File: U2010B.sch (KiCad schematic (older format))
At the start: 27 parts, among them J1 PHASE, J2 M2, J3 Rsh, J4 Rsh, J5 NULL, J6 M1, P1 50k, Q1 BT136-600, U1 U2010B

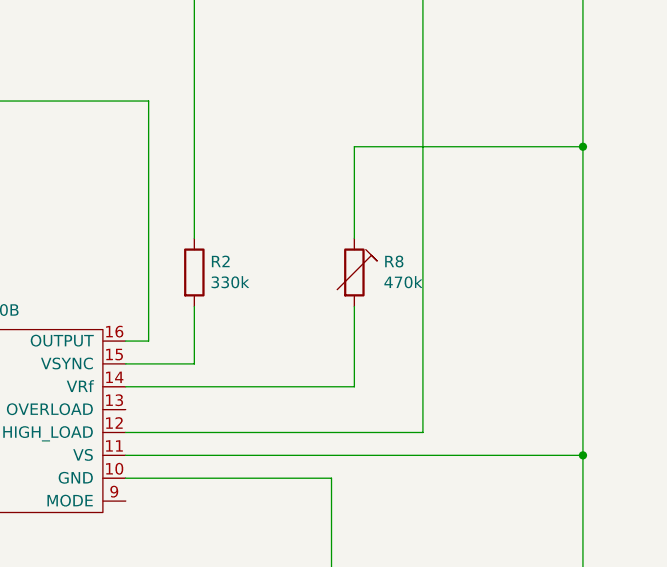
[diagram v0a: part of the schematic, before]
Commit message: Trace PCB
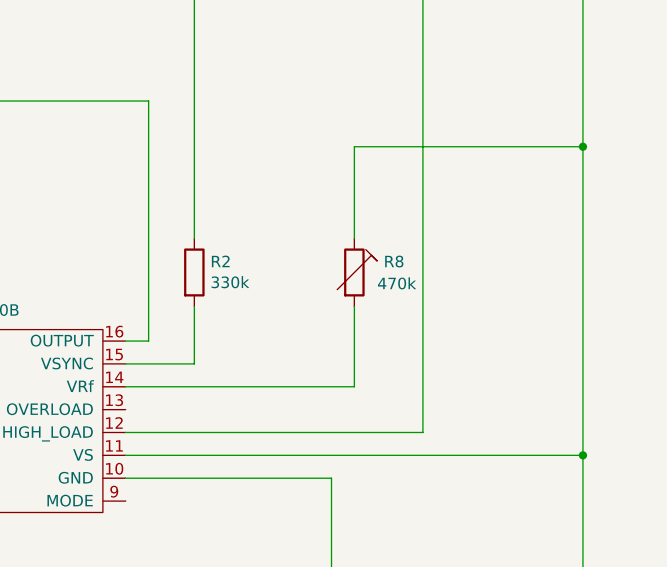
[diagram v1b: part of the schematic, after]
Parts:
- R10, R11, R8: footprint Potentiometer_THT:Potentiometer_Vishay_T7-YA_Single_Vertical -> Potentiometer_THT:Potentiometer_Bourns_3339P_Vertical_HandSoldering
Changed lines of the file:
@@
 P 7800 3350
 F 0 "R8" H 7928 3396 50  0000 L CNN
-F 1 "470k" H 7928 3305 50  0000 L CNN
-F 2 "Potentiometer_THT:Potentiometer_Vishay_T7-YA_Single_Vertical" V 7730 3350 50  0001 C CNN
+F 1 "470k" H 7900 3300 50  0000 L CNN
+F 2 "Potentiometer_THT:Potentiometer_Bourns_3339P_Vertical_HandSoldering" V 7730 3350 50  0001 C CNN
 F 3 "~" H 7800 3350 50  0001 C CNN
 	1    7800 3350
@@
 F 0 "R10" V 4150 5050 50  0000 C CNN
 F 1 "100k" V 4250 5100 50  0000 C CNN
-F 2 "Potentiometer_THT:Potentiometer_Vishay_T7-YA_Single_Vertical" V 3980 5150 50  0001 C CNN
+F 2 "Potentiometer_THT:Potentiometer_Bourns_3339P_Vertical_HandSoldering" V 3980 5150 50  0001 C CNN
 F 3 "~" H 4050 5150 50  0001 C CNN
 	1    4050 5150
@@
 F 0 "R11" V 4650 4300 50  0000 C CNN
 F 1 "1M" V 4650 4550 50  0000 C CNN
-F 2 "Potentiometer_THT:Potentiometer_Vishay_T7-YA_Single_Vertical" V 4680 4450 50  0001 C CNN
+F 2 "Potentiometer_THT:Potentiometer_Bourns_3339P_Vertical_HandSoldering" V 4680 4450 50  0001 C CNN
 F 3 "~" H 4750 4450 50  0001 C CNN
 	1    4750 4450

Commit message: Add netlist, change some pins for drill.
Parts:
- C1: footprint Capacitor_THT:CP_Radial_D6.3mm_P2.50mm -> Capacitor_THT:CP_Radial_D10.0mm_P3.80mm
- C2, C7: footprint Capacitor_THT:CP_Radial_D6.3mm_P2.50mm -> Capacitor_THT:CP_Radial_D8.0mm_P3.80mm
- D3: footprint LED_THT:LED_D3.0mm -> LED_THT:LED_D5.0mm
- J1, J2, J3, J4, J5, J6: footprint Connector_Pin:Pin_D1.0mm_L10.0mm -> Connector_Wire:SolderWirePad_1x01_Drill2mm
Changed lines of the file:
@@
 F 0 "D3" H 8443 2166 50  0000 C CNN
 F 1 "LED" H 8443 2075 50  0000 C CNN
-F 2 "LED_THT:LED_D3.0mm" H 8450 1950 50  0001 C CNN
+F 2 "LED_THT:LED_D5.0mm" H 8450 1950 50  0001 C CNN
 F 3 "~" H 8450 1950 50  0001 C CNN
 	1    8450 1950
@@
 F 0 "J5" H 2992 5835 50  0000 C CNN
 F 1 "NULL" H 2992 5744 50  0000 C CNN
-F 2 "Connector_Pin:Pin_D1.0mm_L10.0mm" H 3100 5650 50  0001 C CNN
+F 2 "Connector_Wire:SolderWirePad_1x01_Drill2mm" H 3100 5650 50  0001 C CNN
 F 3 "~" H 3100 5650 50  0001 C CNN
 	1    3100 5650
@@
 F 0 "C2" H 5218 4496 50  0000 L CNN
 F 1 "4.7u" H 5218 4405 50  0000 L CNN
-F 2 "Capacitor_THT:CP_Radial_D6.3mm_P2.50mm" H 5138 4300 50  0001 C CNN
+F 2 "Capacitor_THT:CP_Radial_D8.0mm_P3.80mm" H 5138 4300 50  0001 C CNN
 F 3 "~" H 5100 4450 50  0001 C CNN
 	1    5100 4450
@@
 F 0 "C7" H 5482 5104 50  0000 R CNN
 F 1 "1u" H 5482 5195 50  0000 R CNN
-F 2 "Capacitor_THT:CP_Radial_D6.3mm_P2.50mm" H 5638 5000 50  0001 C CNN
+F 2 "Capacitor_THT:CP_Radial_D8.0mm_P3.80mm" H 5638 5000 50  0001 C CNN
 F 3 "~" H 5600 5150 50  0001 C CNN
 	1    5600 5150
@@
 F 0 "C1" H 8682 4854 50  0000 R CNN
 F 1 "22u" H 8682 4945 50  0000 R CNN
-F 2 "Capacitor_THT:CP_Radial_D6.3mm_P2.50mm" H 8838 4750 50  0001 C CNN
+F 2 "Capacitor_THT:CP_Radial_D10.0mm_P3.80mm" H 8838 4750 50  0001 C CNN
 F 3 "~" H 8800 4900 50  0001 C CNN
 	1    8800 4900
@@
 F 0 "J3" H 2992 3075 50  0000 C CNN
 F 1 "Rsh" H 2992 3166 50  0000 C CNN
-F 2 "Connector_Pin:Pin_D1.0mm_L10.0mm" H 3100 3300 50  0001 C CNN
+F 2 "Connector_Wire:SolderWirePad_1x01_Drill2mm" H 3100 3300 50  0001 C CNN
 F 3 "~" H 3100 3300 50  0001 C CNN
 	1    3100 3300
@@
 F 0 "J4" H 2992 3525 50  0000 C CNN
 F 1 "Rsh" H 2992 3616 50  0000 C CNN
-F 2 "Connector_Pin:Pin_D1.0mm_L10.0mm" H 3100 3750 50  0001 C CNN
+F 2 "Connector_Wire:SolderWirePad_1x01_Drill2mm" H 3100 3750 50  0001 C CNN
 F 3 "~" H 3100 3750 50  0001 C CNN
 	1    3100 3750
@@
 F 0 "J1" H 2992 1425 50  0000 C CNN
 F 1 "PHASE" H 2992 1516 50  0000 C CNN
-F 2 "Connector_Pin:Pin_D1.0mm_L10.0mm" H 3100 1650 50  0001 C CNN
+F 2 "Connector_Wire:SolderWirePad_1x01_Drill2mm" H 3100 1650 50  0001 C CNN
 F 3 "~" H 3100 1650 50  0001 C CNN
 	1    3100 1650
@@
 F 0 "J2" H 3050 1850 50  0000 C CNN
 F 1 "M2" H 3150 1950 50  0000 C CNN
-F 2 "Connector_Pin:Pin_D1.0mm_L10.0mm" H 3100 1950 50  0001 C CNN
+F 2 "Connector_Wire:SolderWirePad_1x01_Drill2mm" H 3100 1950 50  0001 C CNN
 F 3 "~" H 3100 1950 50  0001 C CNN
 	1    3100 1950
@@
 F 0 "J6" H 3050 2150 50  0000 C CNN
 F 1 "M1" H 3150 2050 50  0000 C CNN
-F 2 "Connector_Pin:Pin_D1.0mm_L10.0mm" H 3100 2050 50  0001 C CNN
+F 2 "Connector_Wire:SolderWirePad_1x01_Drill2mm" H 3100 2050 50  0001 C CNN
 F 3 "~" H 3100 2050 50  0001 C CNN
 	1    3100 2050
